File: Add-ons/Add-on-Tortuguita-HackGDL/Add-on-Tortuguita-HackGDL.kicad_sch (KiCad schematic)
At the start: 0 parts

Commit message: feat(Hw):Update_Route_And_Init_Addon_Tortuguita
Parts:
- added BT1: Battery_Cell, Footprints:BAT-HLD-001, symbol Device:Battery_Cell
- added C1: 0.1uF, Capacitor_SMD:C_0805_2012Metric, symbol Device:C_Small
- added D1, D2, D3, D4, D5: Red, LED_SMD:LED_0805_2012Metric, symbol Device:LED_Small
- added J1: Conn_02x03_Odd_Even, Footprints:B-2100N06P-B111_CKM, symbol Connector_Generic:Conn_02x03_Odd_Even
- added R1, R2, R3, R4, R5: 330R, Resistor_SMD:R_0805_2012Metric, symbol Device:R_Small
- added SW1: SW_RST, Button_Switch_SMD:SW_SPST_TL3342, symbol Switch:SW_Push
- added SW2: On, Footprints:MSK12C02, symbol Switch:SW_DPDT_x2
- added U1: PY32F002AA15M6TU, Footprints:PY32F002AA15M, symbol MCU_PY32F002:PY32F002AA15M6TU
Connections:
- new net: D3.1 (K), R3.2
- new net: D1.1 (K), R1.2
- new net: D4.1 (K), R4.2
- new net: D5.1 (K), R5.2
- new net: D2.1 (K), R2.2
- new net: BT1.1 (-), SW2.2 (B)
- new net +3.3V: BT1.2 (+), C1.1, J1.6 (Pin_6), U1.1 (VCC)
- new net GND: C1.2, J1.5 (Pin_5), R1.1, R2.1, R3.1, R4.1, R5.1, SW1.1, SW2.1 (A), SW2.4 (C), U1.10 (GND)
- new net NRST: SW1.2, U1.4 (PA0/PF2-NRST)
- new net PA1: D4.2 (A), U1.5 (PA1)
- new net PA5: D2.2 (A), U1.3 (PA5/PF1-OSCOUT)
- new net PA6: D1.2 (A), U1.6 (PA6)
- new net PA7: D5.2 (A), U1.7 (PA7)
- new net PF0: D3.2 (A), U1.2 (PF0-OSCIN)
- new net SWCLK: J1.2 (Pin_2), U1.9 (PA14-SWC/PB3)
- new net SWDIO: J1.1 (Pin_1), U1.8 (PA13-SWD)
- no-connect marks 0 -> 3
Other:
- note added: "Battery"
- note added: "LED"
- note added: "Microcontroller"
- note added: "RST"
- note added: "Shitty Add-on"

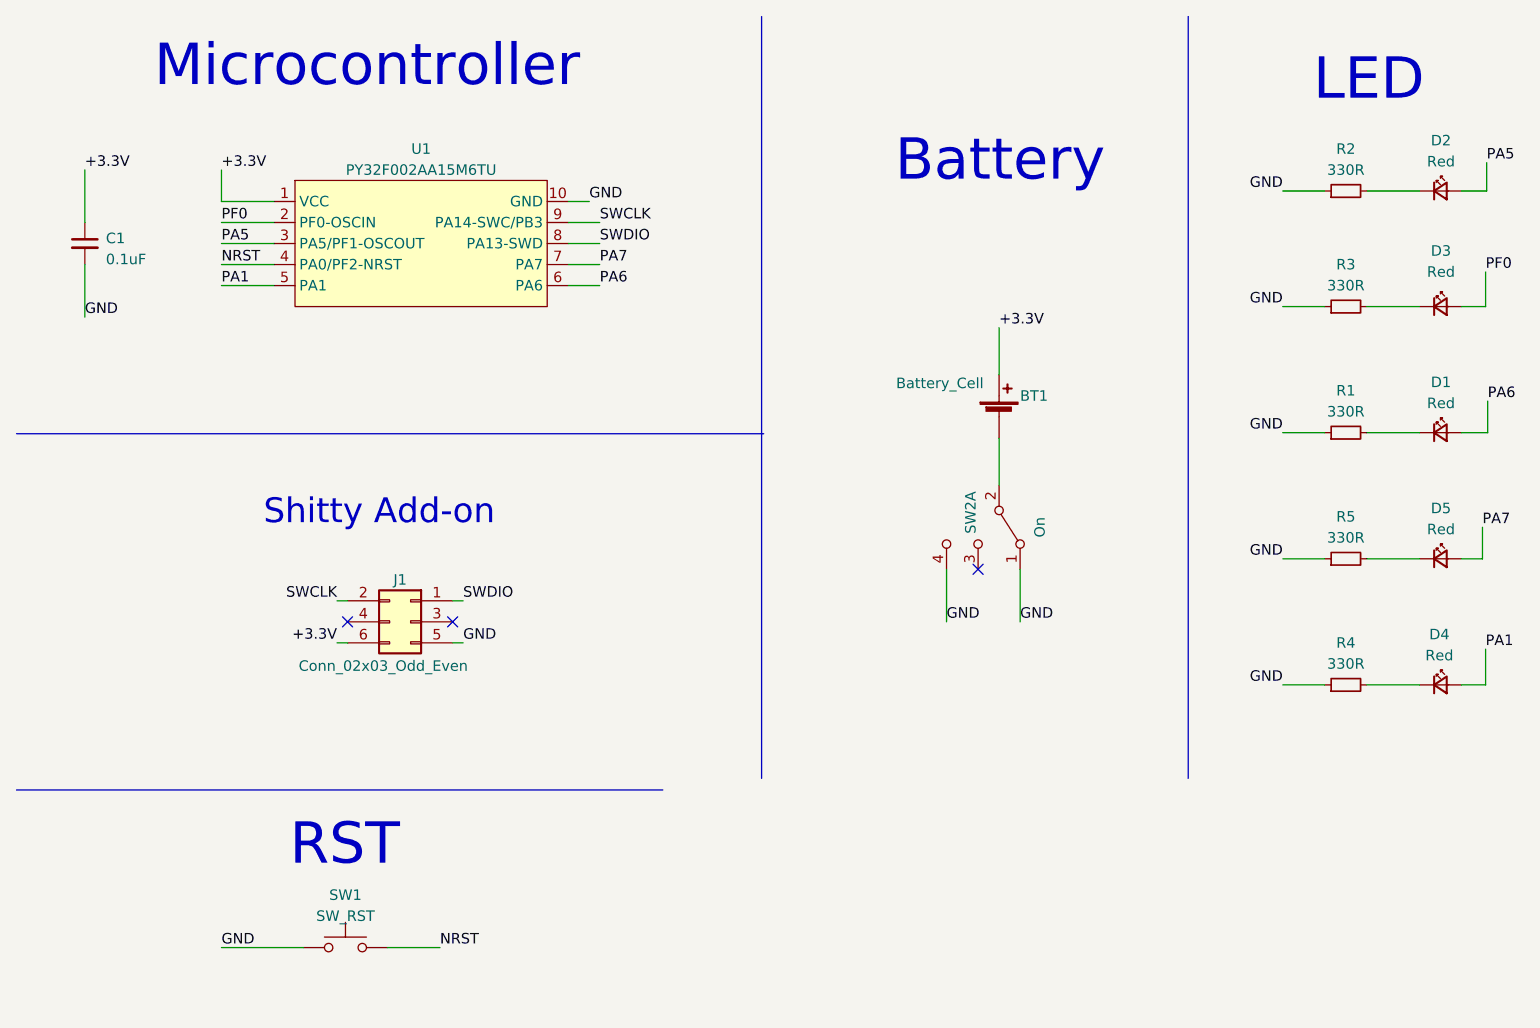
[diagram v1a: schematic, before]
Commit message: feat(Hw):Update_Labels
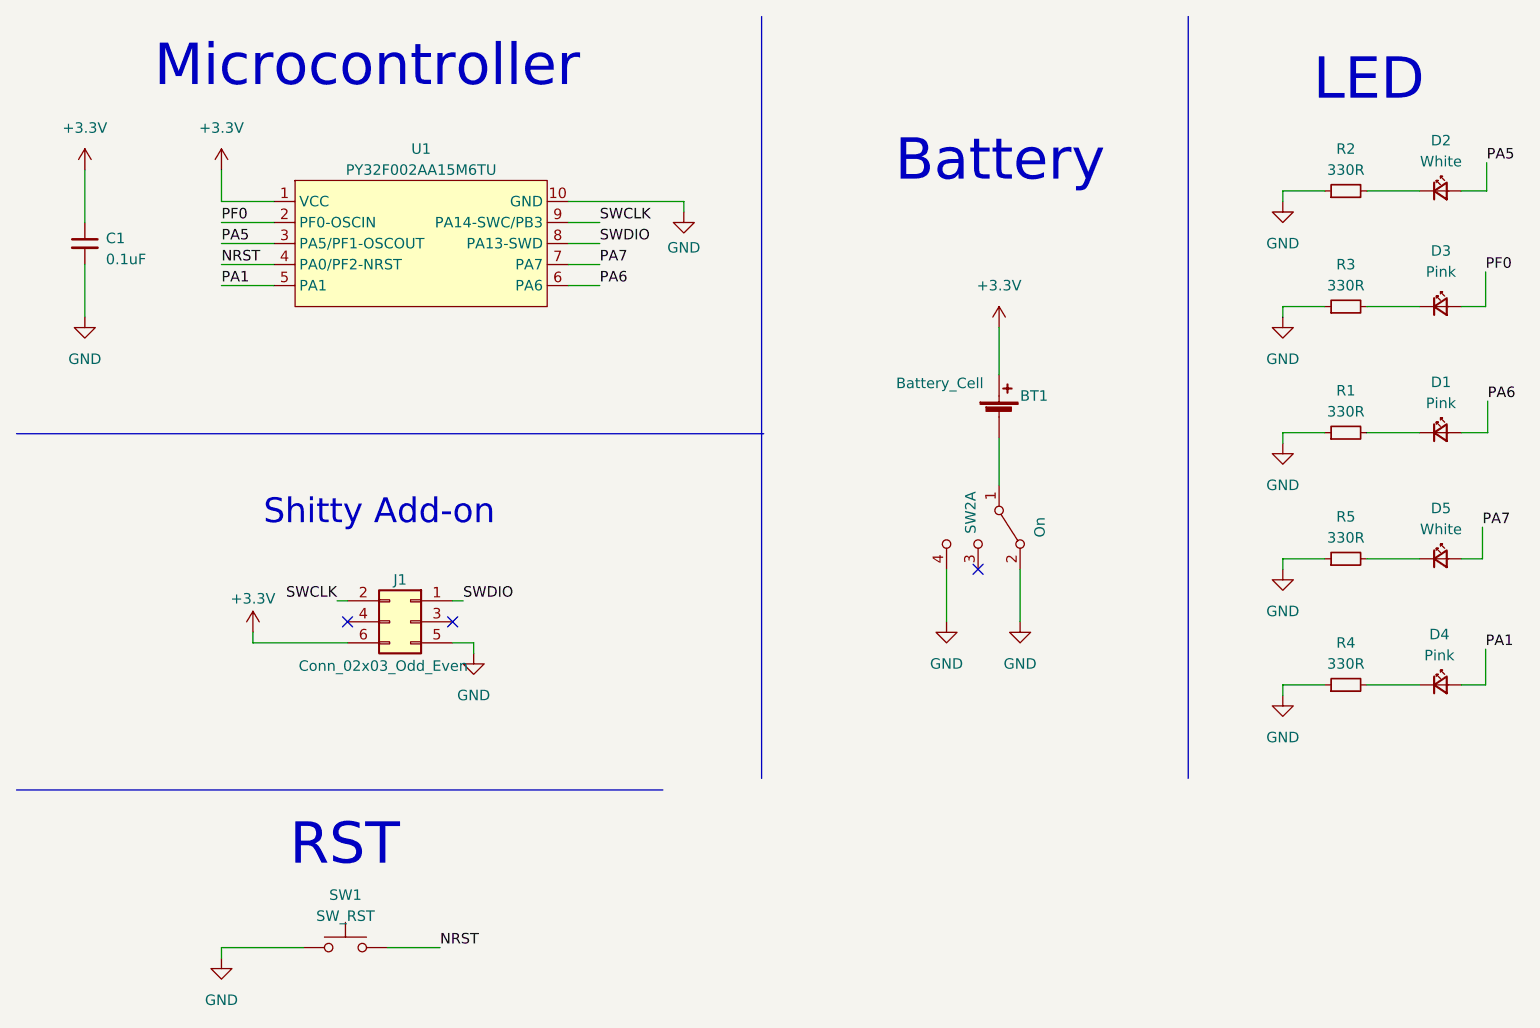
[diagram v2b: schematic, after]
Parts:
- D1, D3, D4: value Red -> Pink; LCSC# C965812 -> C965821
- D2, D5: value Red -> White; LCSC# C965812 -> C84258
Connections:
- net GND: now also SW2.2 (A); no longer SW2.1 (A)
- net at BT1.1 (-): now also SW2.1 (B); no longer SW2.2 (B)
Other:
- company: (none) -> Electronic Cats
- title: (none) -> Add-On-Tortuguita
